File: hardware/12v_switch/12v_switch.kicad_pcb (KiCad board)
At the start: 2 copper layers, 85 parts, among them J1 Screw_Terminal_01x04, J2 Conn_01x06, J3 Conn_01x06, M1 SCREW_6-32_POWER, M10 SCREW_6-32_POWER, M11 SCREW_6-32_POWER, M12 SCREW_6-32_POWER, M13 SCREW_6-32_POWER, M14 SCREW_6-32_POWER, M15 SCREW_6-32_POWER, M16 SCREW_6-32_POWER, M17 SCREW_6-32_POWER, M18 SCREW_6-32_POWER, M19 SCREW_6-32_NORMAL, M2 SCREW_6-32_POWER, M20 SCREW_6-32_NORMAL, M21 SCREW_6-32_NORMAL, M22 SCREW_6-32_NORMAL, M3 SCREW_6-32_POWER, M4 SCREW_6-32_POWER, M5 SCREW_6-32_POWER, M6 SCREW_6-32_POWER, M7 SCREW_6-32_POWER, M8 SCREW_6-32_POWER, M9 SCREW_6-32_POWER, Q1 INFINEON_IRLML0040TRPBF, Q2 INFINEON_IRLML0040TRPBF, Q3 INFINEON_IRLML0040TRPBF, Q4 INFINEON_IRLML0040TRPBF, Q5 INFINEON_IRLML0040TRPBF, Q6 INFINEON_IRLML0040TRPBF, Q7 INFINEON_IRLML0040TRPBF, Q8 INFINEON_IRLML0040TRPBF, U1 TI_LM5111-1MX_NOPB, U2 TI_LM5111-1MX_NOPB, U3 TI_LM5111-1MX_NOPB, U4 DIRTBAG_QUICKBUCK, U5 TI_LM5111-1MX_NOPB, U8 TI_TCAN334GDR, U9 SPARKFUN_COM-18357

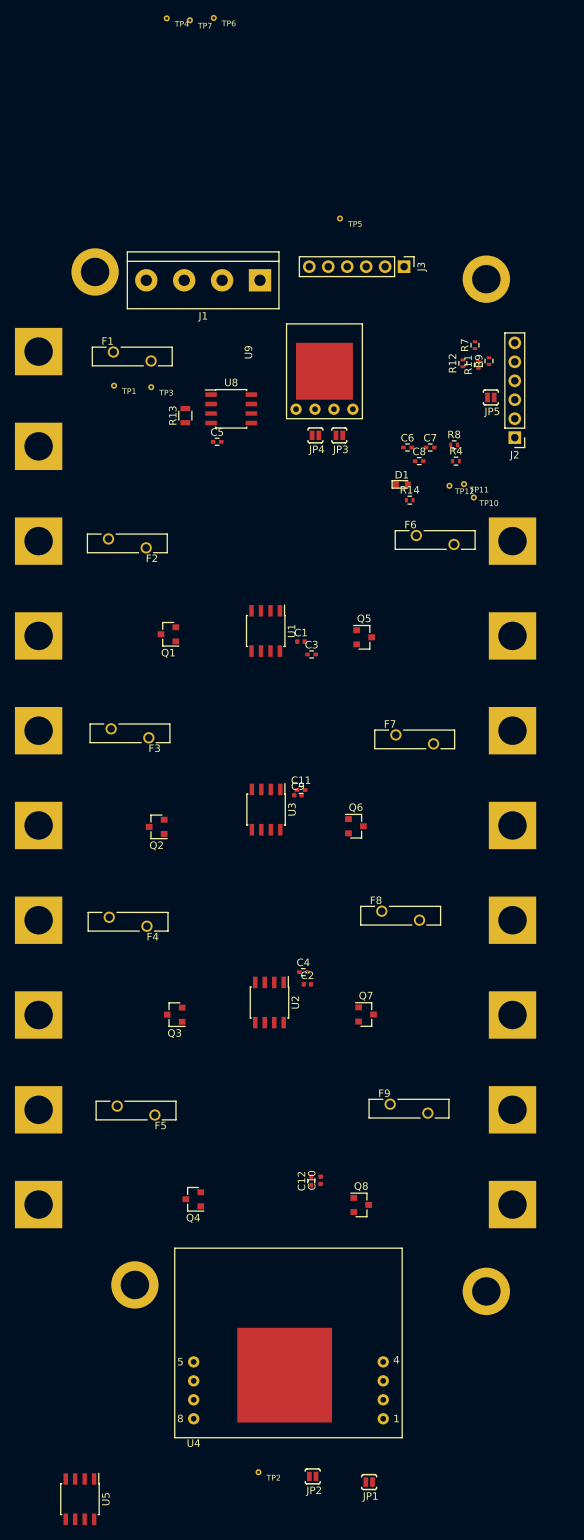
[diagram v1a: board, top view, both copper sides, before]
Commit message: First draft layout with 4 switches + buck
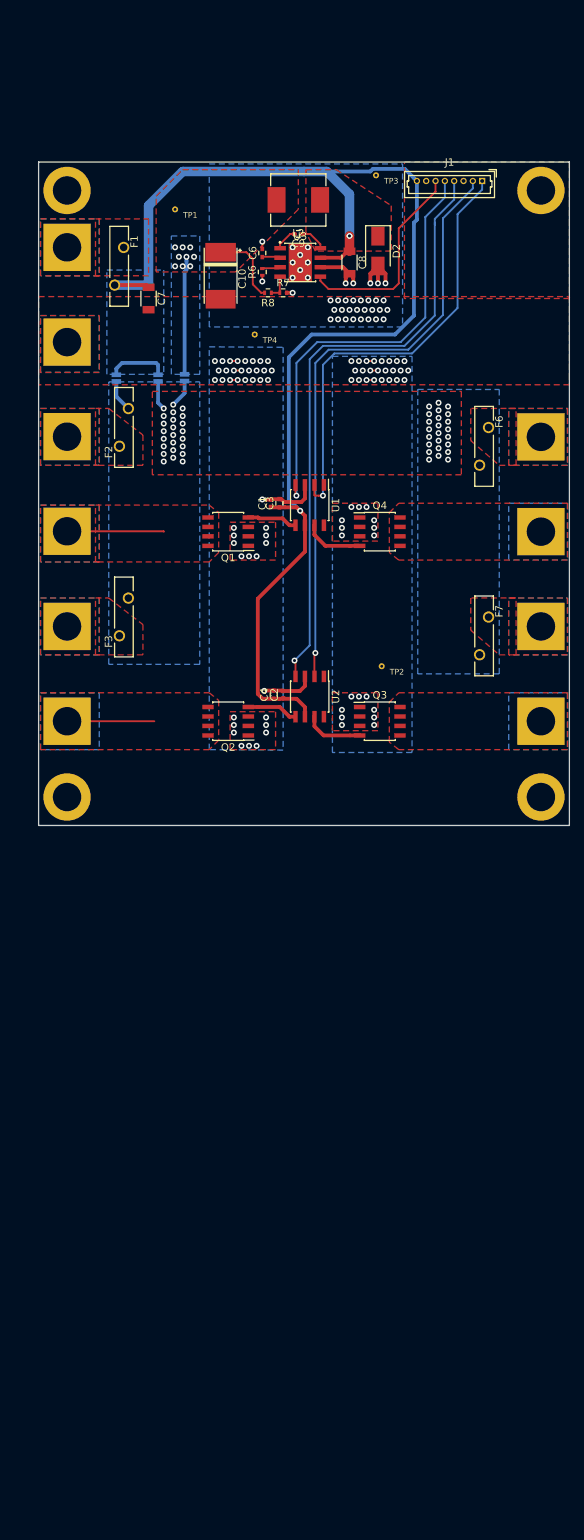
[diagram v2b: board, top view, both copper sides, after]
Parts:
- removed C11, C12: MURATA_GRM155R71H104ME14J, Capacitors_SMD:C_0402
- removed C5: MURATA_GCM155R71C104KA55J, Capacitors_SMD:C_0402
- removed D1: INOLUX_IN-S63BTR, LEDs:LED_0603
- removed F4, F5, F8, F9: LITTLEFUSE_RGEF300-2, DBLS_Misc:LITTLEFUSE_RGEF
- removed J2, J3: Conn_01x06, Pin_Headers:Pin_Header_Straight_1x06_Pitch2.54mm
- removed JP4, JP5: PAD_JUMPER_2PIN_NC, DBLS_Misc:PAD_JUMPER_2PIN_NC
- removed M10, M15, M16, M17, M18, M7, M8, M9: SCREW_6-32_POWER, DBLS_Mechanical:SCREW_6-32_POWER
- removed Q5, Q6, Q7, Q8: INFINEON_IRLML0040TRPBF, TO_SOT_Packages_SMD:SOT-23
- removed R11, R12: VISHAYDALE_CRCW040233R0JNEDC, Resistors_SMD:R_0402
- removed R13: VISHAYDALE_RCS0805120RJNEA, Resistors_SMD:R_0805
- removed R14: VISHAYDALE_CRCW0402620RJNED, Resistors_SMD:R_0402
- removed R4: VISHAYDALE_CRCW040210K0FKED, Resistors_SMD:R_0402
- removed R9: VISHAYDALE_CRCW0402100KJNEDC, Resistors_SMD:R_0402
- removed TP10, TP11, TP12: DBLS_TESTPOINT_NORMAL, DBLS_Misc:DBLS_Testpoint_Normal
- removed the TP2 at (54.9, 201.0)
- removed the TP3 at (40.5, 55.6)
- removed the TP4 at (42.6, 6.15)
- removed U4: DIRTBAG_QUICKBUCK, DBLS_Misc:DBLS_QuickBuck
- removed U5: TI_LM5111-1MX_NOPB, Housings_SOIC:SOIC-8_3.9x4.9mm_Pitch1.27mm
- removed U8: TI_TCAN334GDR, Housings_SOIC:SOIC-8_3.9x4.9mm_Pitch1.27mm
- removed U9: SPARKFUN_COM-18357, DBLS_Misc:SPARKFUN_BABYBUCK
- added D2: VISHAY_SSA33L-E3_61T, Diodes_SMD:D_SMA, F.Cu at (70.9, 37.3)
- added L2: PANASONIC_ETQ-P3M100KVN, DBLS_Inductor:L_6.4x6.0_H3, F.Cu at (60.2, 30.5)
- added R6: VISHAYDALE_CRCW04020000Z0EDHP, Resistors_SMD:R_0402, F.Cu at (55.4, 40.1)
- C10: value SMD-CAP-1UF-0402 -> VISHAY_593D107X0020E2TE3; footprint DBLS_Capacitor:C_0402_1005Metric -> DBLS_Capacitor:C_2917
- C7: value MURATA_GCM155R71C104KA55J -> MURATA_GRM31CC81E226KE11L; footprint Capacitors_SMD:C_0402 -> Capacitors_SMD:C_1206
- C8: value MURATA_GCM155R71C104KA55J -> MURATA_GRT31CR61H106KE01L; footprint Capacitors_SMD:C_0402 -> Capacitors_SMD:C_1206
- C9: value SMD-CAP-1UF-0402 -> MURATA_GCM155R71E103KA37D; footprint DBLS_Capacitor:C_0402_1005Metric -> Capacitors_SMD:C_0402
- J1: value Screw_Terminal_01x04 -> MOLEX_0530470810; footprint Connectors:bornier4 -> Connectors_Molex:Molex_PicoBlade_53047-0810_08x1.25mm_Straight
- JP1, JP2, JP3: moved to B.Cu
- Q1, Q2, Q3, Q4: value INFINEON_IRLML0040TRPBF -> INFINEON_IRF7470TRPBF; footprint TO_SOT_Packages_SMD:SOT-23 -> Housings_SOIC:SOIC-8_3.9x4.9mm_Pitch1.27mm
- R7: value VISHAYDALE_CRCW0402100KJNEDC -> VISHAYDALE_CRCW04025K60JNED
- R8: value VISHAYDALE_CRCW040210K0FKED -> VISHAYDALE_CRCW04022K00JNEDC
- U3: value TI_LM5111-1MX_NOPB -> TI_LM22680QMRE-ADJ; footprint Housings_SOIC:SOIC-8_3.9x4.9mm_Pitch1.27mm -> DBLS_SOIC:SOIC-8-1EP_3.9x4.9mm_Pitch1.27mm_ALT
- moved JP1 151.8 mm to (35.8, 54.4), turned to 270 degrees
- moved JP2 148.6 mm to (41.4, 54.4), turned to 270 degrees
- moved C10 121.9 mm to (49.8, 40.6), turned to 270 degrees
- moved Q4 92.9 mm to (71.1, 74.9), turned to 0 degrees
- moved C9 75.2 mm to (60.2, 35.1), turned to 180 degrees
- moved U3 73.4 mm to (60.5, 38.9), turned to 0 degrees
- moved M20 66.6 mm to (92.7, 110.5)
- moved M21 66.0 mm to (29.2, 110.5)
- moved TP2 60.3 mm to (71.4, 93.0)
- moved Q3 48.0 mm to (71.1, 100.3), turned to 0 degrees
- moved TP4 43.0 mm to (54.4, 48.5)
- moved C7 42.7 mm to (40.1, 43.7), turned to 270 degrees
- moved U2 41.3 mm to (61.7, 97.0)
- moved C2 38.9 mm to (58.2, 96.8), turned to 90 degrees
- moved C4 37.4 mm to (56.9, 96.8), turned to 90 degrees
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- renumbered TP5 to TP2, TP6 to TP3, TP7 to TP4
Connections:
- C10 pad 1: +12V -> +5V
- C6 pad 1: +3V3 -> Net-(C6-Pad1)
- C7 pad 1: +3V3 -> +12V
- C8 pad 1: +3V3 -> +12V
- C9 pad 1: +12V -> Net-(C9-Pad1)
- C9 pad 2: GND -> Net-(C9-Pad2)
- F2 pad 1: +12V -> Net-(F2-Pad1)
- F2 pad 2: Net-(F2-Pad2) -> VBUS
- F3 pad 1: +12V -> Net-(F3-Pad1)
- F3 pad 2: Net-(F3-Pad2) -> VBUS
- F6 pad 1: +5V -> Net-(F6-Pad1)
- F6 pad 2: Net-(F6-Pad2) -> VBUS
- F7 pad 1: +5V -> Net-(F7-Pad1)
- F7 pad 2: Net-(F7-Pad2) -> VBUS
- J1 pad 1: +12V -> /PWM4
- J1 pad 2: /CAN1_H -> /PWM3
- J1 pad 3: /CAN1_L -> GND
- J1 pad 4: GND -> /PWM2
- JP1 pad 2: Net-(JP1-Pad2) -> VBUS
- JP2 pad 1: Net-(JP2-Pad1) -> +12V
- JP2 pad 2: +5V -> VBUS
- JP3 pad 1: +3V3 -> +5V
- JP3 pad 2: Net-(JP3-Pad2) -> VBUS
- M11 pad 1: Net-(F6-Pad2) -> Net-(F6-Pad1)
- M13 pad 1: Net-(F7-Pad2) -> Net-(F7-Pad1)
- M3 pad 1: Net-(F2-Pad2) -> Net-(F2-Pad1)
- M5 pad 1: Net-(F3-Pad2) -> Net-(F3-Pad1)
- Q1 pad 1: Net-(Q1-Pad1) -> GND
- Q1 pad 3: Net-(M4-Pad1) -> GND
- Q2 pad 1: Net-(Q2-Pad1) -> GND
- Q2 pad 3: Net-(M6-Pad1) -> GND
- Q3 pad 1: Net-(Q3-Pad1) -> GND
- Q3 pad 3: Net-(M8-Pad1) -> GND
- Q4 pad 1: Net-(Q4-Pad1) -> GND
- Q4 pad 3: Net-(M10-Pad1) -> GND
- R7 pad 1: /UART_RX -> Net-(R7-Pad1)
- R7 pad 2: +3V3 -> GND
- R8 pad 1: +3V3 -> Net-(R7-Pad1)
- R8 pad 2: /NRST -> +5V
- TP1 pad 1: +BATT -> +5V
- U1 pad 2: /PWM1 -> /PWM4
- U1 pad 4: /PWM2 -> /PWM1
- U1 pad 5: Net-(Q2-Pad1) -> Net-(Q1-Pad4)
- U1 pad 7: Net-(Q1-Pad1) -> Net-(Q4-Pad4)
- U2 pad 2: /PWM1 -> /PWM3
- U2 pad 5: Net-(Q4-Pad1) -> Net-(Q2-Pad4)
- U2 pad 7: Net-(Q3-Pad1) -> Net-(Q3-Pad4)
- U3 pad 1: Net-(U3-Pad1) -> Net-(C9-Pad2)
- U3 pad 2: /PWM5 -> Net-(C6-Pad1)
- U3 pad 3: GND -> Net-(R6-Pad2)
- U3 pad 4: /PWM6 -> Net-(R7-Pad1)
- U3 pad 5: Net-(Q6-Pad1) -> /5V_ENABLE
- U3 pad 6: +12V -> GND
- U3 pad 7: Net-(Q5-Pad1) -> +12V
- U3 pad 8: Net-(U3-Pad8) -> Net-(C9-Pad1)
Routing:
- net +12V: track 0.00 -> 184.2 mm, vias 0 -> 2
- net /PWM2: track 0.00 -> 82.0 mm, vias 0 -> 1
- net /PWM3: track 0.00 -> 81.4 mm, vias 0 -> 1
- net /PWM4: track 0.00 -> 59.6 mm, vias 0 -> 1
- net /PWM1: track 0.00 -> 58.4 mm, vias 0 -> 1
- net GND: track 0.00 -> 39.2 mm, vias 0 -> 126
- net /5V_ENABLE: track 0.00 -> 27.6 mm
- net +5V: track 0.00 -> 26.0 mm, vias 0 -> 9
- net Net-(M4-Pad1): track 0.00 -> 13.0 mm
- net VBUS: track 0.00 -> 12.0 mm, vias 0 -> 48
- net Net-(M6-Pad1): track 0.00 -> 11.7 mm
- net Net-(Q4-Pad4): track 0.00 -> 7.96 mm
- net Net-(Q3-Pad4): track 0.00 -> 7.85 mm
- net Net-(Q2-Pad4): track 0.00 -> 6.86 mm
- net Net-(Q1-Pad4): track 0.00 -> 6.75 mm
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- added copper zone on B.Cu, net +12V
- added copper zone on B.Cu, net +5V
- added copper zone on F.Cu, net +5V
- added copper zone on B.Cu, net +BATT
- added copper zone on F.Cu, net +BATT
- added copper zone on B.Cu, net GND
- added copper zone on F.Cu, net GND
- added copper zone on F.Cu, net Net-(C9-Pad1)
- added copper zone on B.Cu, net Net-(F2-Pad1)
- added copper zone on F.Cu, net Net-(F2-Pad1)
- added copper zone on B.Cu, net Net-(F3-Pad1)
- added copper zone on F.Cu, net Net-(F3-Pad1)
- added copper zone on B.Cu, net Net-(F6-Pad1)
- added copper zone on F.Cu, net Net-(F6-Pad1)
- added copper zone on B.Cu, net Net-(F7-Pad1)
- added copper zone on F.Cu, net Net-(F7-Pad1)
- added copper zone on B.Cu, net Net-(M12-Pad1)
- added copper zone on F.Cu, net Net-(M12-Pad1)
- added copper zone on B.Cu, net Net-(M14-Pad1)
- added copper zone on F.Cu, net Net-(M14-Pad1)
- added copper zone on B.Cu, net Net-(M4-Pad1)
- added copper zone on F.Cu, net Net-(M4-Pad1)
- added copper zone on B.Cu, net Net-(M6-Pad1)
- added copper zone on F.Cu, net Net-(M6-Pad1)
- added copper zone on B.Cu, net VBUS
- added copper zone on F.Cu, net VBUS
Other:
- board outline added: 71.1 x 88.9 mm

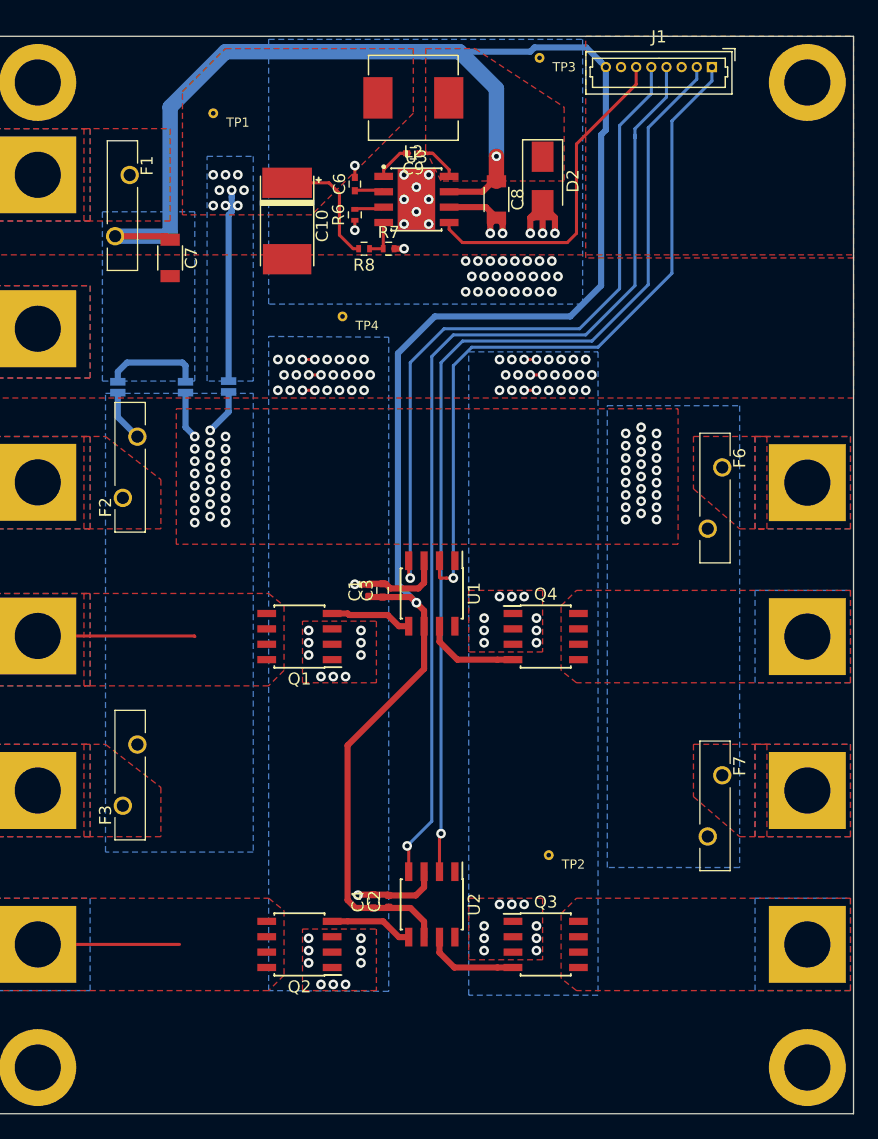
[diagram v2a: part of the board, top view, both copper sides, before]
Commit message: fixed designators. Added logo and labels
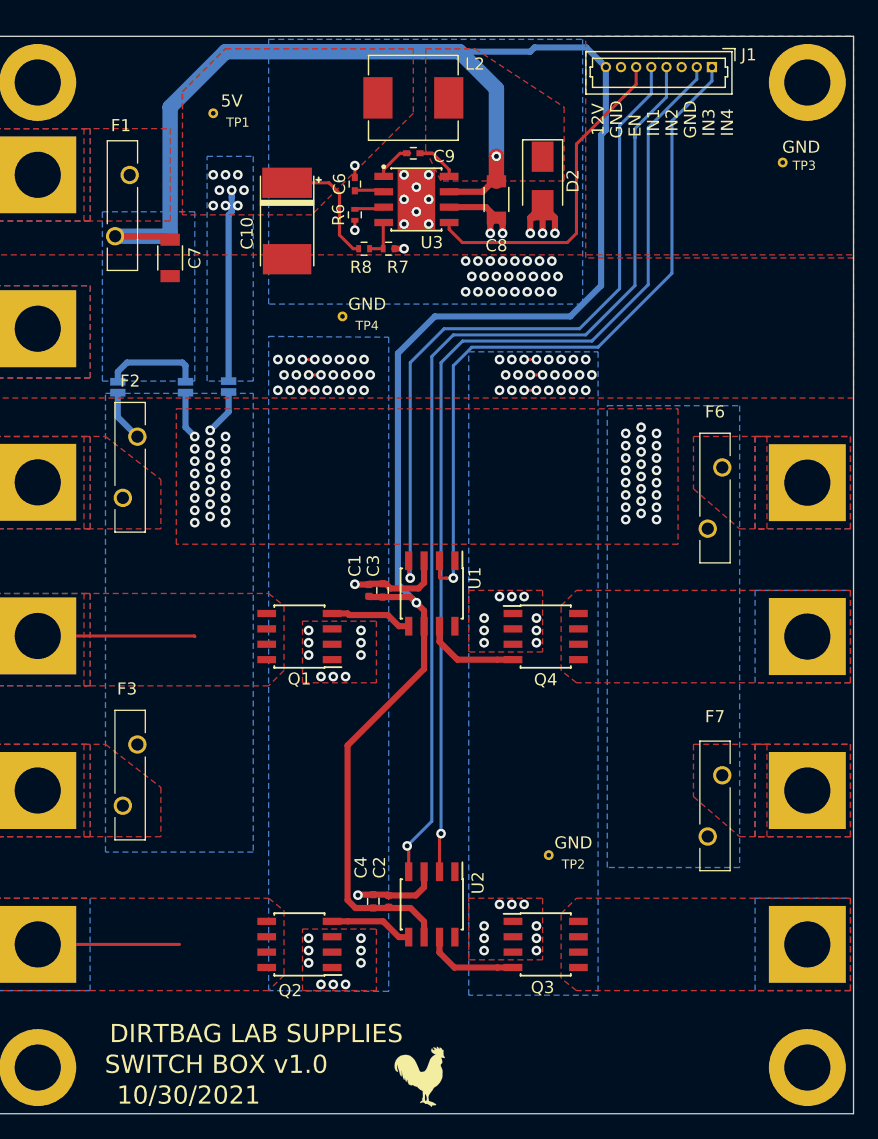
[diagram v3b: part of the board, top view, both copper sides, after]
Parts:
- added G***: LOGO, DBLS_LOGO:Rooster_43mmx43mm, B.Cu at (62.0, 72.4)
- added LOGO1: DBLS_Chicken_Small, DBLS_LOGO:Rooster_4mmx4mm, F.Cu at (60.7, 111.3)
- moved TP3 21.8 mm to (90.7, 35.8)
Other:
- board text added: "10/30/2021"
- board text added: "12V"
- board text added: "5V"
- board text added: "DIRTBAG LAB SUPPLIES"
- board text added: "EN"
- board text added: "GND"
- board text added: "IN1"
- board text added: "IN2"
- board text added: "IN3"
- board text added: "IN4"
- board text added: "SWITCH BOX v1.0"

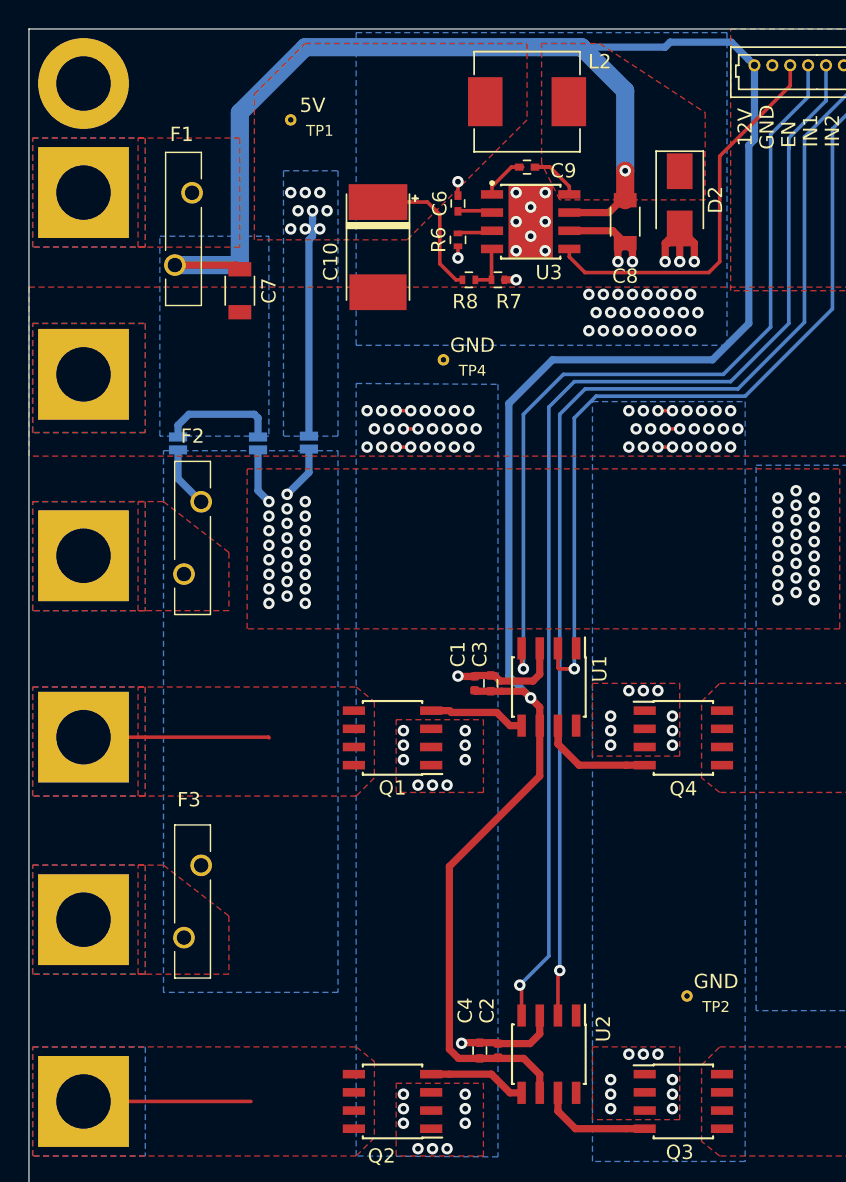
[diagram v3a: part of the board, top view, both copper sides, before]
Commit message: added reverse polarity, TVS, and better regulator bypass cap, and fixed feedback resistors
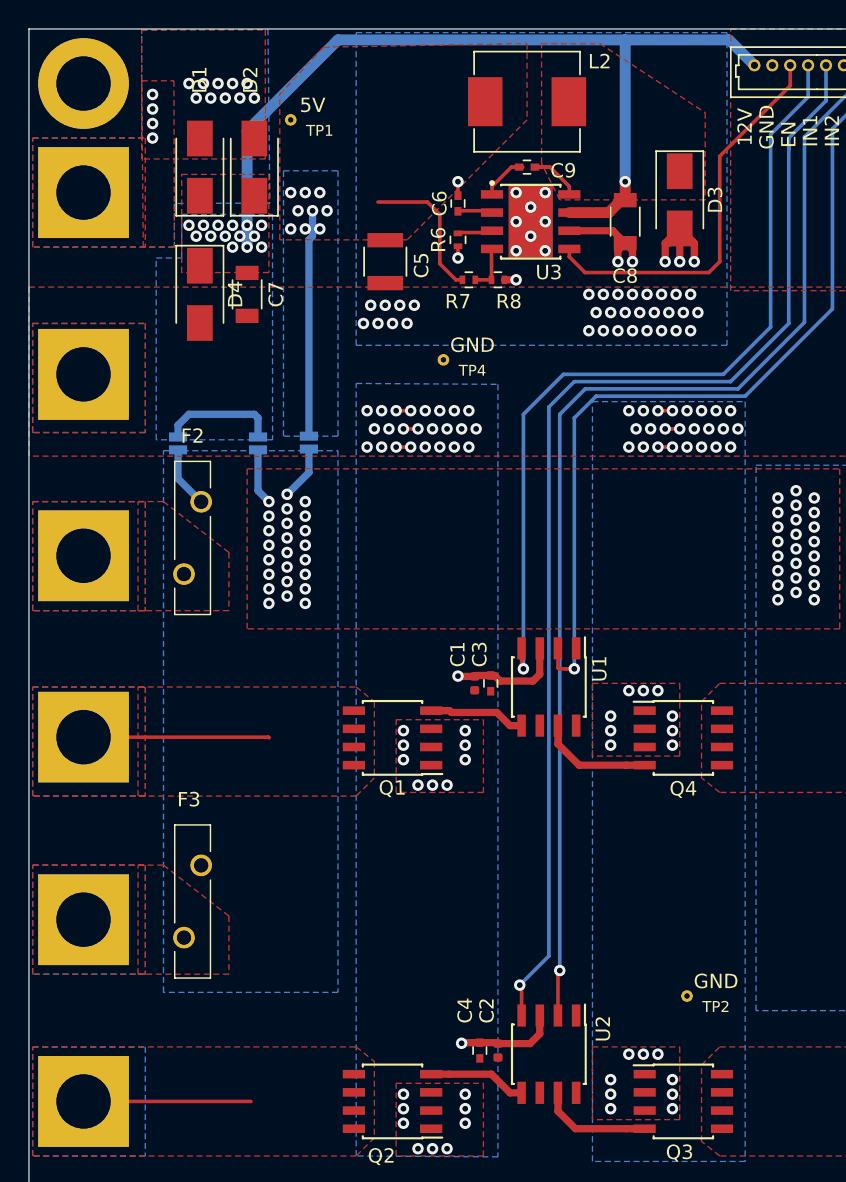
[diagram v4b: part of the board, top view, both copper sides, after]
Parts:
- removed C10: VISHAY_593D107X0020E2TE3, DBLS_Capacitor:C_2917
- removed F1: LITTLEFUSE_RGEF700-2, DBLS_Misc:LITTLEFUSE_RGEF
- removed G***: LOGO, DBLS_LOGO:Rooster_43mmx43mm
- added C5: TAIYO-YUDEN_LMK325ABJ107MM-P, Capacitors_SMD:C_1210, F.Cu at (50.3, 41.7)
- added D1: VISHAY_SSA34HE3_A_I, Diodes_SMD:D_SMA, F.Cu at (37.3, 35.1)
- added D3: VISHAY_SSA34HE3_A_I, Diodes_SMD:D_SMA, F.Cu at (70.9, 37.3)
- added D4: LITTLEFUSE_TPSMA6L20A, Diodes_SMD:D_SMA, F.Cu at (37.3, 43.9)
- D2: value VISHAY_SSA33L-E3_61T -> VISHAY_SSA34HE3_A_I
- moved D2 29.8 mm to (41.1, 35.1), turned to 90 degrees
- moved R7 2.03 mm to (56.1, 42.9)
- moved R8 2.03 mm to (58.2, 42.9), turned to 0 degrees
- moved C7 0.57 mm to (40.6, 43.9)
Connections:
- D2 pad 1: Net-(C9-Pad1) -> +12V
- D2 pad 2: GND -> +BATT
- R7 pad 1: Net-(R7-Pad1) -> +5V
- R7 pad 2: GND -> Net-(R7-Pad2)
- R8 pad 1: Net-(R7-Pad1) -> Net-(R7-Pad2)
- R8 pad 2: +5V -> GND
- U3 pad 4: Net-(R7-Pad1) -> Net-(R7-Pad2)
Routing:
- net +12V: track 184.2 -> 70.6 mm, vias 2 -> 15
- net Net-(R7-Pad2): track 0.00 -> 3.31 mm
- net Net-(R7-Pad1): track 3.31 -> 0.00 mm
- net +BATT: vias 0 -> 14
- net (no net): vias 0 -> 8
- added copper zone on F.Cu, net +12V
